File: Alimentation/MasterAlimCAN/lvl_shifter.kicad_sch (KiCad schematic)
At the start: 3 parts, among them Q1 BSS138

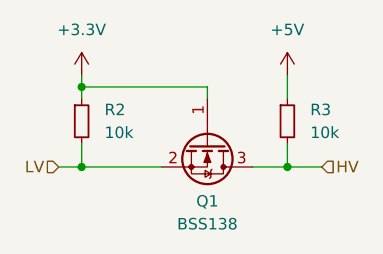
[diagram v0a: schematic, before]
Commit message: Restructure schematics of AlimCAN
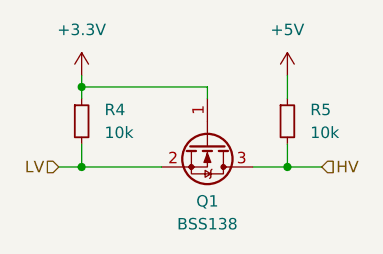
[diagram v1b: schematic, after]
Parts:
- renumbered R2 to R4, R3 to R5
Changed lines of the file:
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@@
   (symbol (lib_id "power:+5V") (at 156.21 73.66 0) (unit 1)
     (in_bom yes) (on_board yes) (dnp no) (fields_autoplaced)
-    (property "Reference" "#PWR021" (at 156.21 77.47 0)
+    (property "Reference" "#PWR028" (at 156.21 77.47 0)
       (effects (font (size 1.27 1.27)) hide)
     )
@@
     (instances
       (project "MasterAlimCAN"
-        (path "/c83bc042-587c-48f9-abdb-41233c8ec938/3da43f86-0520-4797-8d8a-f370cac20cce"
-          (reference "#PWR021") (unit 1)
+        (path "/c83bc042-587c-48f9-abdb-41233c8ec938/a4b1e0da-5816-453f-b06d-61ca2c30c9c0/695f7ad9-57c2-4a4f-bb6c-c509d5b85b6e"
+          (reference "#PWR028") (unit 1)
         )
-        (path "/c83bc042-587c-48f9-abdb-41233c8ec938/089105fe-c96c-467a-9c54-c49136cd48fd"
-          (reference "#PWR024") (unit 1)
+        (path "/c83bc042-587c-48f9-abdb-41233c8ec938/a4b1e0da-5816-453f-b06d-61ca2c30c9c0/45ba4592-3283-40ac-88e5-837ad2ebe39d"
+          (reference "#PWR030") (unit 1)
         )
       )
@@
   (symbol (lib_id "Device:R_Small") (at 156.21 78.74 0) (unit 1)
     (in_bom yes) (on_board yes) (dnp no) (fields_autoplaced)
-    (property "Reference" "R3" (at 158.75 77.47 0)
+    (property "Reference" "R5" (at 158.75 77.47 0)
       (effects (font (size 1.27 1.27)) (justify left))
     )
@@
     (instances
       (project "MasterAlimCAN"
-        (path "/c83bc042-587c-48f9-abdb-41233c8ec938/3da43f86-0520-4797-8d8a-f370cac20cce"
-          (reference "R3") (unit 1)
+        (path "/c83bc042-587c-48f9-abdb-41233c8ec938/a4b1e0da-5816-453f-b06d-61ca2c30c9c0/695f7ad9-57c2-4a4f-bb6c-c509d5b85b6e"
+          (reference "R5") (unit 1)
         )
-        (path "/c83bc042-587c-48f9-abdb-41233c8ec938/089105fe-c96c-467a-9c54-c49136cd48fd"
-          (reference "R5") (unit 1)
+        (path "/c83bc042-587c-48f9-abdb-41233c8ec938/a4b1e0da-5816-453f-b06d-61ca2c30c9c0/45ba4592-3283-40ac-88e5-837ad2ebe39d"
+          (reference "R7") (unit 1)
         )
       )
@@
     (instances
       (project "MasterAlimCAN"
-        (path "/c83bc042-587c-48f9-abdb-41233c8ec938/3da43f86-0520-4797-8d8a-f370cac20cce"
+        (path "/c83bc042-587c-48f9-abdb-41233c8ec938/a4b1e0da-5816-453f-b06d-61ca2c30c9c0/695f7ad9-57c2-4a4f-bb6c-c509d5b85b6e"
           (reference "Q1") (unit 1)
         )
-        (path "/c83bc042-587c-48f9-abdb-41233c8ec938/089105fe-c96c-467a-9c54-c49136cd48fd"
+        (path "/c83bc042-587c-48f9-abdb-41233c8ec938/a4b1e0da-5816-453f-b06d-61ca2c30c9c0/45ba4592-3283-40ac-88e5-837ad2ebe39d"
           (reference "Q2") (unit 1)
         )
@@
   (symbol (lib_id "Device:R_Small") (at 133.35 78.74 0) (unit 1)
     (in_bom yes) (on_board yes) (dnp no) (fields_autoplaced)
-    (property "Reference" "R2" (at 135.89 77.47 0)
+    (property "Reference" "R4" (at 135.89 77.47 0)
       (effects (font (size 1.27 1.27)) (justify left))
     )
@@
     (instances
       (project "MasterAlimCAN"
-        (path "/c83bc042-587c-48f9-abdb-41233c8ec938/3da43f86-0520-4797-8d8a-f370cac20cce"
-          (reference "R2") (unit 1)
+        (path "/c83bc042-587c-48f9-abdb-41233c8ec938/a4b1e0da-5816-453f-b06d-61ca2c30c9c0/695f7ad9-57c2-4a4f-bb6c-c509d5b85b6e"
+          (reference "R4") (unit 1)
         )
-        (path "/c83bc042-587c-48f9-abdb-41233c8ec938/089105fe-c96c-467a-9c54-c49136cd48fd"
-          (reference "R4") (unit 1)
+        (path "/c83bc042-587c-48f9-abdb-41233c8ec938/a4b1e0da-5816-453f-b06d-61ca2c30c9c0/45ba4592-3283-40ac-88e5-837ad2ebe39d"
+          (reference "R6") (unit 1)
         )
       )
@@
   (symbol (lib_id "power:+3.3V") (at 133.35 73.66 0) (unit 1)
     (in_bom yes) (on_board yes) (dnp no) (fields_autoplaced)
-    (property "Reference" "#PWR022" (at 133.35 77.47 0)
+    (property "Reference" "#PWR027" (at 133.35 77.47 0)
       (effects (font (size 1.27 1.27)) hide)
     )
@@
     (instances
       (project "MasterAlimCAN"
-        (path "/c83bc042-587c-48f9-abdb-41233c8ec938/3da43f86-0520-4797-8d8a-f370cac20cce"
-          (reference "#PWR022") (unit 1)
+        (path "/c83bc042-587c-48f9-abdb-41233c8ec938/a4b1e0da-5816-453f-b06d-61ca2c30c9c0/695f7ad9-57c2-4a4f-bb6c-c509d5b85b6e"
+          (reference "#PWR027") (unit 1)
         )
-        (path "/c83bc042-587c-48f9-abdb-41233c8ec938/089105fe-c96c-467a-9c54-c49136cd48fd"
-          (reference "#PWR023") (unit 1)
+        (path "/c83bc042-587c-48f9-abdb-41233c8ec938/a4b1e0da-5816-453f-b06d-61ca2c30c9c0/45ba4592-3283-40ac-88e5-837ad2ebe39d"
+          (reference "#PWR029") (unit 1)
         )
       )

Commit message: Init placement for MasterAlimCAN
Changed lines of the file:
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@@
   (junction (at 133.35 74.93) (diameter 0) (color 0 0 0 0)
+  )
+  (junction (at 156.21 83.82) (diameter 0) (color 0 0 0 0)
   )
   (junction (at 133.35 83.82) (diameter 0) (color 0 0 0 0)
   )
-  (junction (at 156.21 83.82) (diameter 0) (color 0 0 0 0)
+  (wire (pts (xy 156.21 73.66) (xy 156.21 76.2))
+    (stroke (width 0) (type default))
   )
-  (wire (pts (xy 156.21 73.66) (xy 156.21 76.2))
+  (wire (pts (xy 152.4 83.82) (xy 156.21 83.82))
     (stroke (width 0) (type default))
   )
@@
     (stroke (width 0) (type default))
   )
+  (wire (pts (xy 133.35 83.82) (xy 142.24 83.82))
+    (stroke (width 0) (type default))
+  )
   (wire (pts (xy 133.35 73.66) (xy 133.35 74.93))
     (stroke (width 0) (type default))
   )
-  (wire (pts (xy 147.32 76.2) (xy 147.32 74.93))
+  (wire (pts (xy 147.32 74.93) (xy 147.32 76.2))
     (stroke (width 0) (type default))
   )
   (wire (pts (xy 133.35 74.93) (xy 133.35 76.2))
-    (stroke (width 0) (type default))
-  )
-  (wire (pts (xy 152.4 83.82) (xy 156.21 83.82))
-    (stroke (width 0) (type default))
-  )
-  (wire (pts (xy 142.24 83.82) (xy 133.35 83.82))
     (stroke (width 0) (type default))
   )
@@
   (symbol (lib_id "power:+5V") (at 156.21 73.66 0) (unit 1)
     (in_bom yes) (on_board yes) (dnp no) (fields_autoplaced)
-    (property "Reference" "#PWR028" (at 156.21 77.47 0)
+    (property "Reference" "#PWR030" (at 156.21 77.47 0)
       (effects (font (size 1.27 1.27)) hide)
     )
@@
       (project "MasterAlimCAN"
         (path "/c83bc042-587c-48f9-abdb-41233c8ec938/a4b1e0da-5816-453f-b06d-61ca2c30c9c0/695f7ad9-57c2-4a4f-bb6c-c509d5b85b6e"
-          (reference "#PWR028") (unit 1)
+          (reference "#PWR030") (unit 1)
         )
         (path "/c83bc042-587c-48f9-abdb-41233c8ec938/a4b1e0da-5816-453f-b06d-61ca2c30c9c0/45ba4592-3283-40ac-88e5-837ad2ebe39d"
-          (reference "#PWR030") (unit 1)
+          (reference "#PWR032") (unit 1)
         )
       )
@@
     )
   )
-  (symbol (lib_id "Transistor_FET:BSS138") (at 147.32 81.28 270) (unit 1)
+  (symbol (lib_name "BSS138_1") (lib_id "Transistor_FET:BSS138") (at 147.32 81.28 270) (unit 1)
     (in_bom yes) (on_board yes) (dnp no) (fields_autoplaced)
     (property "Reference" "Q1" (at 147.32 87.63 90)
@@
       (effects (font (size 1.27 1.27) italic) (justify left) hide)
     )
-    (property "Datasheet" "https://www.onsemi.com/pub/Collateral/BSS138-D.PDF" (at 147.32 81.28 0)
+    (property "Datasheet" "https://www.onsemi.com/pub/Collateral/BSS138-D.PDF" (at 143.51 86.36 0)
       (effects (font (size 1.27 1.27)) (justify left) hide)
     )
@@
       (effects (font (size 1.27 1.27)) hide)
     )
+    (pin "3")
     (pin "2")
-    (pin "3")
     (pin "1")
     (instances
@@
   (symbol (lib_id "power:+3.3V") (at 133.35 73.66 0) (unit 1)
     (in_bom yes) (on_board yes) (dnp no) (fields_autoplaced)
-    (property "Reference" "#PWR027" (at 133.35 77.47 0)
+    (property "Reference" "#PWR029" (at 133.35 77.47 0)
       (effects (font (size 1.27 1.27)) hide)
     )
@@
       (project "MasterAlimCAN"
         (path "/c83bc042-587c-48f9-abdb-41233c8ec938/a4b1e0da-5816-453f-b06d-61ca2c30c9c0/695f7ad9-57c2-4a4f-bb6c-c509d5b85b6e"
-          (reference "#PWR027") (unit 1)
+          (reference "#PWR029") (unit 1)
         )
         (path "/c83bc042-587c-48f9-abdb-41233c8ec938/a4b1e0da-5816-453f-b06d-61ca2c30c9c0/45ba4592-3283-40ac-88e5-837ad2ebe39d"
-          (reference "#PWR029") (unit 1)
+          (reference "#PWR031") (unit 1)
         )
       )
